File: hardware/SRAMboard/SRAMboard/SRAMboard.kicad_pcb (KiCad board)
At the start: 2 copper layers, 0 parts

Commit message: SRAMboard I
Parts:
- added C1: C, Capacitor_SMD:C_0805_2012Metric, F.Cu at (134.7, 70.3)
- added C2: C, Capacitor_SMD:C_0805_2012Metric, F.Cu at (113.0, 70.6)
- added J1: Conn_02x13_Odd_Even, Connector_PinSocket_2.54mm:PinSocket_2x13_P2.54mm_Vertical, F.Cu at (95.4, 61.5)
- added J2: Conn_02x13_Odd_Even, Connector_PinSocket_2.54mm:PinSocket_2x13_P2.54mm_Vertical, F.Cu at (149.9, 63.1)
- added U1: IS66WV51216EBLL-70BLI, kifootp:BGA-48_6.0x8.0mm_Layout6x8_P0.75mm, B.Cu at (124.4, 69.6)
- added U2: IS66WV51216EBLL-70TLI, Package_SO:TSOP-II-44_10.16x18.41mm_P0.8mm, F.Cu at (124.4, 69.7)
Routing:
- net A0: track 0.00 -> 32.7 mm
- net A3: track 0.00 -> 29.2 mm, vias 0 -> 2
- net A2: track 0.00 -> 27.9 mm, vias 0 -> 2
- net A4: track 0.00 -> 27.2 mm, vias 0 -> 2
- net A1: track 0.00 -> 26.6 mm, vias 0 -> 2
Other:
- board outline added: 68.7 x 49.3 mm

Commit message: SRAMboard I
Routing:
- net A6: track 0.00 -> 5.11 mm
- net GND: track 0.00 -> 4.89 mm
- net NC1: track 0.00 -> 4.15 mm
- net IO1: track 0.00 -> 4.11 mm
- net A15: track 0.00 -> 4.02 mm
- net A5: track 0.00 -> 3.96 mm
- net IO3: track 0.00 -> 3.86 mm
- net A7: track 0.00 -> 3.81 mm
- net A14: track 0.00 -> 3.62 mm
- net A16: track 0.00 -> 3.50 mm
- net A11: track 0.00 -> 3.41 mm
- net IO0: track 0.00 -> 3.40 mm
- net A17: track 0.00 -> 3.30 mm
- net IO9: track 0.00 -> 3.28 mm
- net IO2: track 0.00 -> 3.21 mm
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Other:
- net class Default: clearance 0.1524 -> 0.125; trace_width 0.1524 -> 0.125; via_dia 0.6858 -> 0.5; via_drill 0.3302 -> 0.25
- rule pad_to_mask_clearance: 0.0508 -> 0.05
- rule trace_clearance: 0.1524 -> 0.125
- rule trace_min: 0.1524 -> 0.125
- rule via_min_drill: 0.254 -> 0.25
- rule via_min_size: 0.508 -> 0.5

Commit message: SRAMboard I
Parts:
- moved C2 44.0 mm to (156.0, 61.6), turned to 90 degrees
- moved J1 30.4 mm to (123.5, 49.6)
- moved J2 26.8 mm to (173.2, 49.9)
- moved U1 21.0 mm to (143.9, 61.6), turned to 0 degrees
- moved U2 20.9 mm to (143.8, 62.0)
- moved C1 7.70 mm to (133.9, 62.7)
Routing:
- net A5: track 3.96 -> 117.1 mm, vias 0 -> 4
- net GND: track 4.89 -> 101.2 mm, vias 0 -> 4
- net A6: track 5.11 -> 98.7 mm, vias 0 -> 5
- net A17: track 3.30 -> 94.6 mm, vias 0 -> 2
- net A11: track 3.41 -> 62.0 mm, vias 0 -> 2
- net A3: track 32.4 -> 7.26 mm, vias 2 -> 0
- net A0: track 32.7 -> 9.12 mm
- net A2: track 30.3 -> 11.4 mm, vias 2 -> 0
- net IO8: track 2.33 -> 19.3 mm
- net IO11: track 2.83 -> 19.6 mm
- net IO10: track 2.79 -> 19.0 mm
- net IO9: track 3.28 -> 18.5 mm
- net A4: track 29.9 -> 14.6 mm, vias 2 -> 0
- net A7: track 3.81 -> 16.3 mm
- net A16: track 3.50 -> 15.7 mm
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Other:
- board outline removed

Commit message: SRAMboard I
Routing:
- net OE#: track 6.70 -> 178.0 mm, vias 0 -> 5
- net UB#: track 12.5 -> 132.3 mm, vias 0 -> 4
- net IO12: track 11.1 -> 130.6 mm, vias 0 -> 4
- net IO11: track 19.6 -> 126.6 mm, vias 0 -> 3
- net IO13: track 11.5 -> 118.2 mm, vias 0 -> 4
- net IO15: track 12.7 -> 119.3 mm, vias 0 -> 4
- net IO14: track 10.4 -> 115.7 mm, vias 0 -> 4
- net LB#: track 12.2 -> 101.1 mm, vias 0 -> 4
- net A7: track 16.3 -> 100.0 mm, vias 0 -> 5
- net A5: track 117.1 -> 150.6 mm, vias 4 -> 5
- net A3: track 7.26 -> 34.6 mm
- net A17: track 94.6 -> 117.9 mm, vias 2 -> 4
- net A0: track 9.12 -> 32.0 mm
- net GND: track 101.2 -> 112.0 mm, vias 4 -> 6
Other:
- board outline added: 139.7 x 96.1 mm

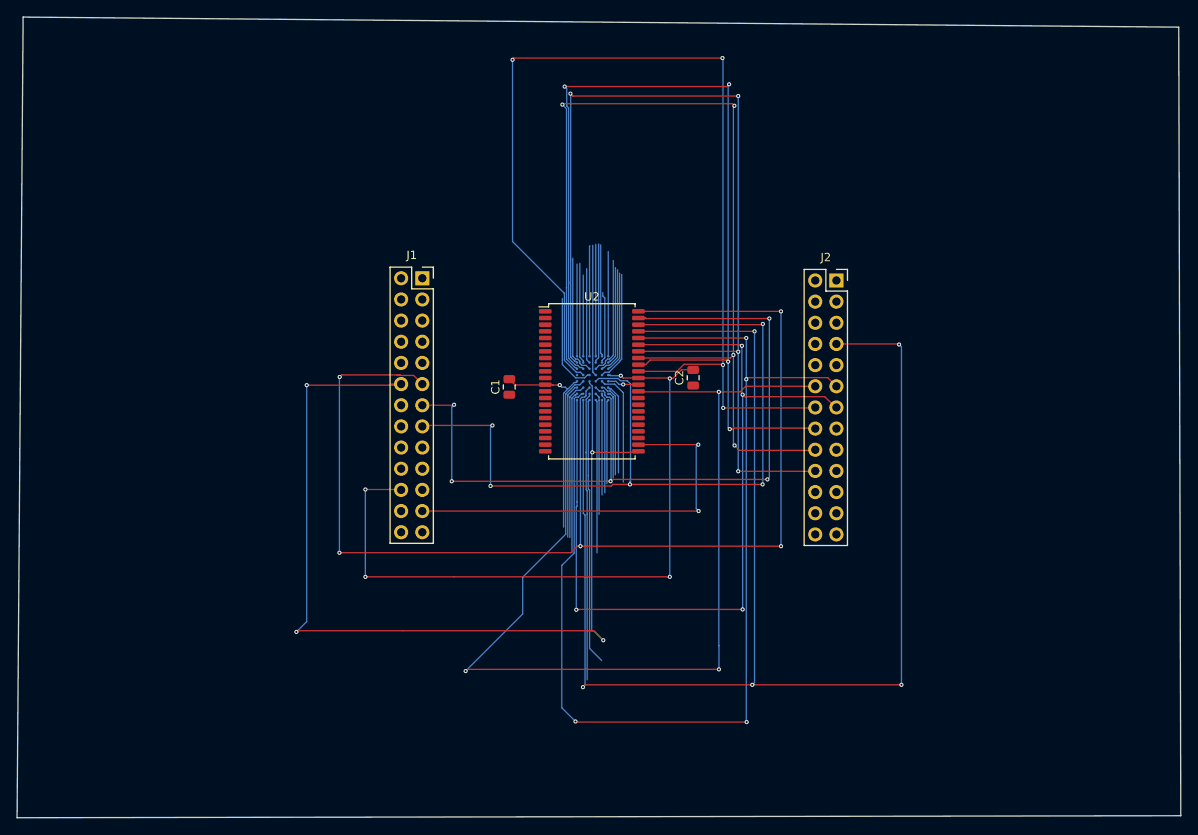
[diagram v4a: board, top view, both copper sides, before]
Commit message: FIXED solder mask issue
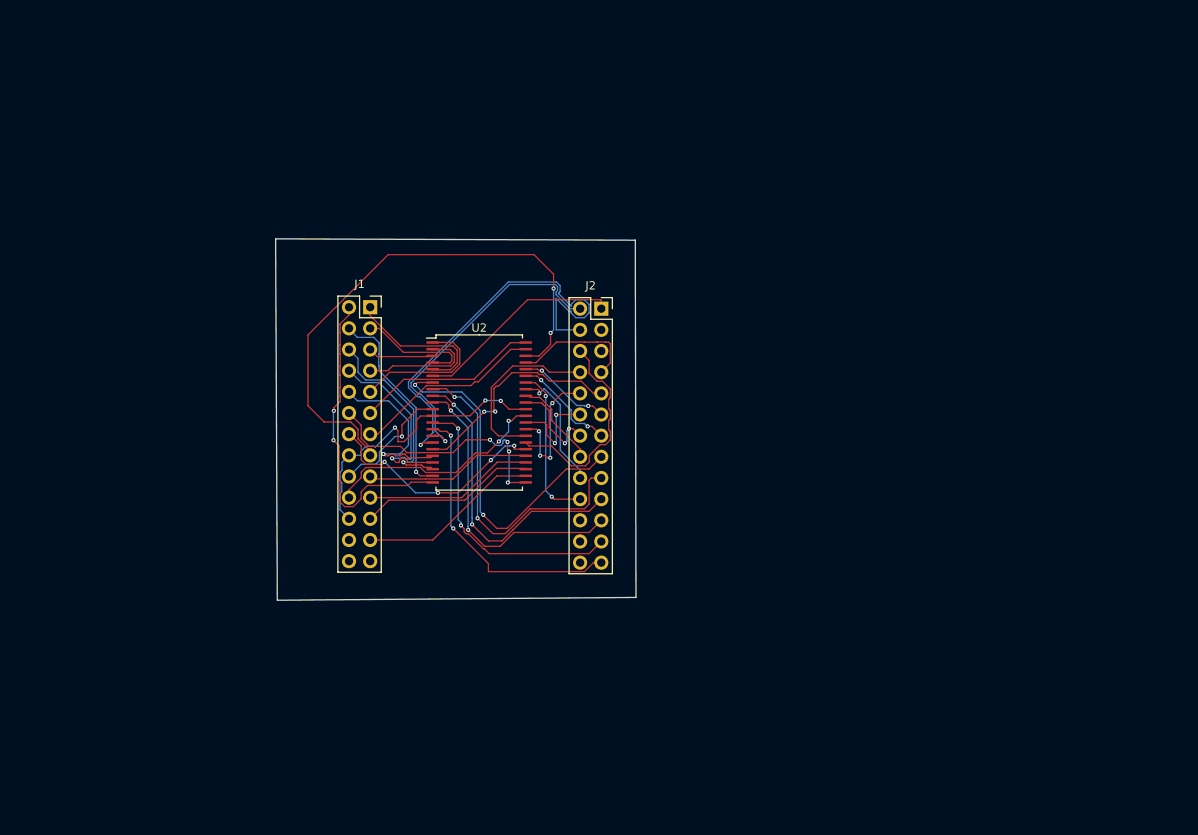
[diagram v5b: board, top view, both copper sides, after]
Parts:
- removed C1, C2: C, Capacitor_SMD:C_0805_2012Metric
- removed U1: IS66WV51216EBLL-70BLI, kifootp:BGA-48_6.0x8.0mm_Layout6x8_P0.75mm
- moved J2 28.4 mm to (145.0, 53.3)
- moved U2 14.0 mm to (130.3, 65.8)
- moved J1 7.15 mm to (117.2, 53.1)
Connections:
- J2 pad 22: NC0 -> Net-(J2-Pad22)
- J2 pad 24: NC1 -> Net-(J2-Pad24)
- J2 pad 26: NC2 -> Net-(J2-Pad26)
- J2 pad 3: CS1# -> Net-(J2-Pad3)
- J2 pad 5: CS2 -> Net-(J2-Pad5)
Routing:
- net OE#: track 178.0 -> 15.2 mm, vias 5 -> 0
- net A5: track 150.6 -> 22.1 mm, vias 5 -> 0
- net UB#: track 132.3 -> 11.5 mm, vias 4 -> 2
- net IO12: track 130.6 -> 11.5 mm, vias 4 -> 2
- net IO11: track 126.6 -> 11.7 mm, vias 3 -> 2
- net IO13: track 118.2 -> 10.5 mm, vias 4 -> 0
- net IO14: track 115.7 -> 15.2 mm, vias 4 -> 1
- net IO15: track 119.3 -> 19.1 mm, vias 4 -> 2
- net LB#: track 101.1 -> 12.6 mm, vias 4 -> 2
- net A17: track 117.9 -> 30.4 mm
- net A6: track 98.7 -> 22.9 mm, vias 5 -> 0
- net GND: track 112.0 -> 36.6 mm, vias 6 -> 3
- net IO7: track 11.8 -> 53.4 mm, vias 0 -> 1
- net A11: track 62.0 -> 21.5 mm, vias 2 -> 0
- net A7: track 100.0 -> 65.8 mm, vias 5 -> 2
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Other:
- board size 139.7 x 96.1 mm -> 43.3 x 43.4 mm
- net class Default: clearance 0.125 -> 0.1524; trace_width 0.125 -> 0.1524
- rule pad_to_mask_clearance: 0.05 -> 0.0508
- rule trace_clearance: 0.125 -> 0.1524
- rule trace_min: 0.125 -> 0.1524
